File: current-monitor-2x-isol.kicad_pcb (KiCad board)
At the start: 2 copper layers, 35 x 44 mm, 34 parts, among them J1 CONN-2, J2 CONN-2, J3 USB-MICROB, J4 JTAG, U1 ACS711EX, U2 ACS711EX, U3 MKL26ZxxVFM4, Y1 12MHz

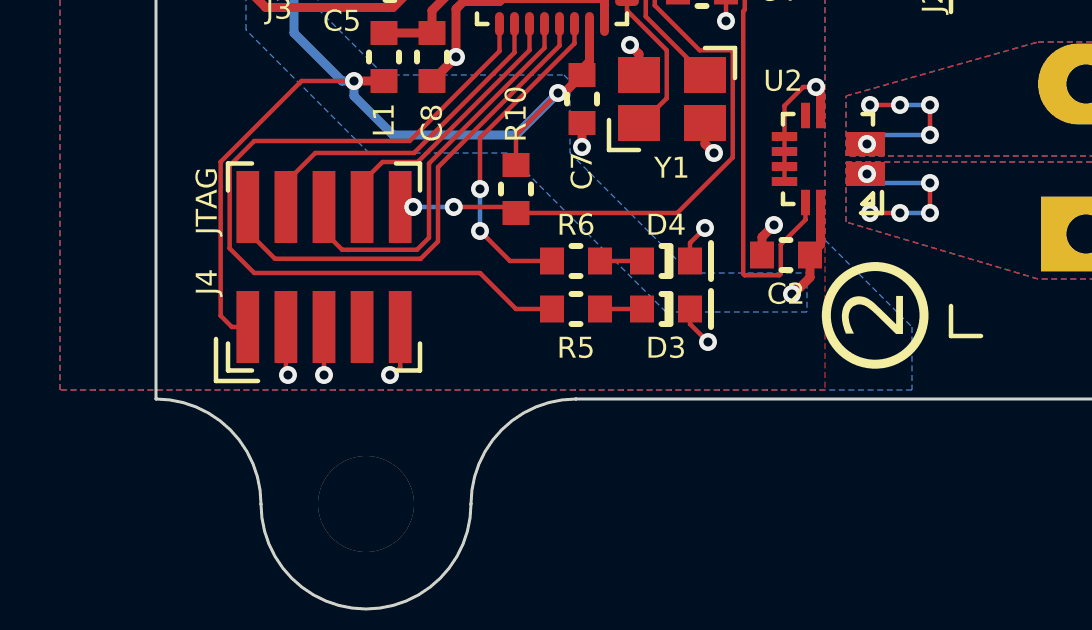
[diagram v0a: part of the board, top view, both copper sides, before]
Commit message: notes, small track change
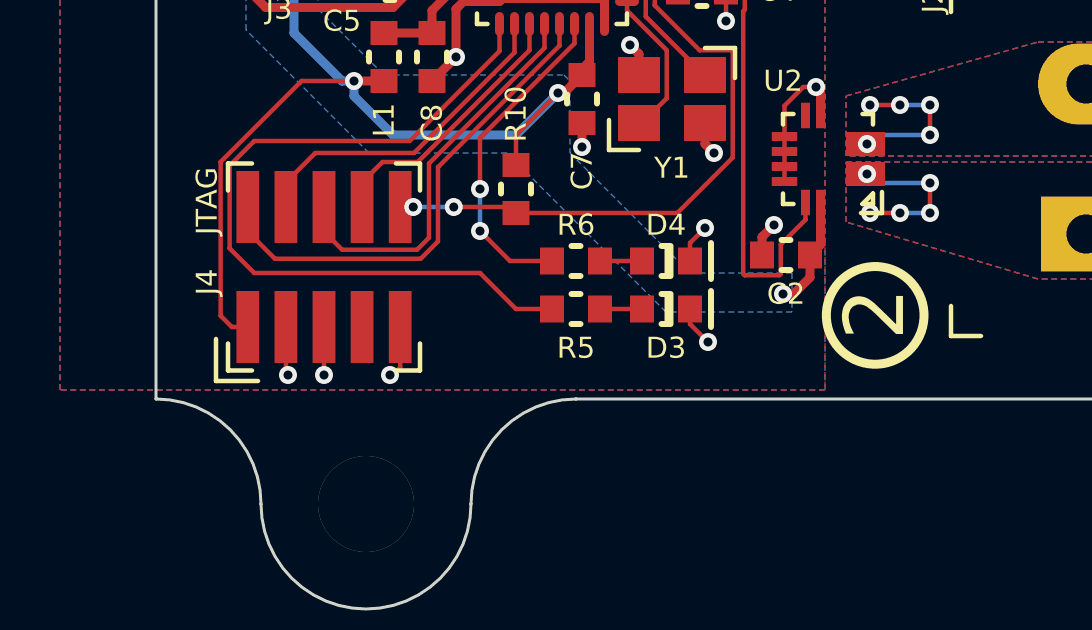
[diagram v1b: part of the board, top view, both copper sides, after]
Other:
- board text added: "70um/2oz copper"
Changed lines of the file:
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@@
     (links 97)
     (no_connects 0)
-    (area 162.949999 75.949999 198.050001 120.050001)
+    (area 109.35 75.799999 198.200001 120.200001)
     (thickness 1.6)
-    (drawings 14)
+    (drawings 15)
     (tracks 317)
     (zones 0)
@@
   (title_block
     (title "2x Isolated Current Monitor")
-    (date 2015-11-09)
+    (date 2015-11-12)
     (rev 1.0)
     (company sternlabs)
@@
     (pad 1 thru_hole circle (at 0 0 180) (size 3.2 3.2) (drill 3.2) (layers *.Cu *.Mask))
   )
+  (gr_text "70um/2oz copper" (at 109.5 83.5) (layer Cmts.User)
+    (effects (font (size 1.5 1.5) (thickness 0.3)) (justify left))
+  )
   (gr_arc (start 170 116.5) (end 173.5 116.5) (angle 180) (layer Edge.Cuts) (width 0.1))
   (gr_arc (start 177 116.5) (end 173.5 116.5) (angle 90) (layer Edge.Cuts) (width 0.1))
@@
   (gr_line (start 163 113) (end 163 83) (layer Edge.Cuts) (width 0.1))
   (gr_line (start 198 83) (end 198 113) (layer Edge.Cuts) (width 0.1))
+  (segment (start 184.25 109.5) (end 183.9 109.5) (width 0.3) (layer F.Cu) (net 1))
+  (segment (start 184.8 108.2) (end 184.8 108.95) (width 0.3) (layer F.Cu) (net 1))
+  (segment (start 184.8 108.95) (end 184.25 109.5) (width 0.3) (layer F.Cu) (net 1))
+  (via (at 183.9 109.5) (size 0.6) (drill 0.3) (layers F.Cu B.Cu) (net 1))
   (segment (start 184.35 95.4) (end 184.1 95.4) (width 0.3) (layer F.Cu) (net 1))
   (segment (start 184.8 94.95) (end 184.35 95.4) (width 0.3) (layer F.Cu) (net 1))
   (segment (start 184.8 94.2) (end 184.8 94.95) (width 0.3) (layer F.Cu) (net 1))
   (via (at 184.1 95.4) (size 0.6) (drill 0.3) (layers F.Cu B.Cu) (net 1))
-  (segment (start 184.25 109.5) (end 184.2 109.5) (width 0.3) (layer F.Cu) (net 1))
-  (segment (start 184.8 108.95) (end 184.25 109.5) (width 0.3) (layer F.Cu) (net 1))
-  (segment (start 184.8 108.2) (end 184.8 108.95) (width 0.3) (layer F.Cu) (net 1))
-  (via (at 184.2 109.5) (size 0.6) (drill 0.3) (layers F.Cu B.Cu) (net 1))
   (segment (start 185.15 106.45) (end 185.15 107.85) (width 0.3) (layer F.Cu) (net 1))
   (segment (start 185.15 107.85) (end 184.8 108.2) (width 0.3) (layer F.Cu) (net 1))
@@
     (polygon
       (pts
-        (xy 159.8 112.7) (xy 159.8 83.3) (xy 185.3 83.3) (xy 185.3 107.7) (xy 188.2 110.6)
-        (xy 188.2 112.7)
+        (xy 159.8 112.7) (xy 159.8 83.3) (xy 185.3 83.3) (xy 185.3 107.7) (xy 185.3 112.7)
       )
     )
@@
       (pts
         (xy 171.4 97) (xy 169 97) (xy 168.4 97.6) (xy 168.4 100) (xy 170.6 102.2)
-        (xy 176.6 102.2) (xy 176.8 102.4) (xy 176.8 104.8) (xy 180.8 108.8) (xy 184.7 108.8)
-        (xy 184.7 110.1) (xy 180 110.1) (xy 174.7 104.8) (xy 170.1 104.8) (xy 166 100.7)
+        (xy 176.6 102.2) (xy 176.8 102.4) (xy 176.8 104.8) (xy 180.8 108.8) (xy 184.2 108.8)
+        (xy 184.2 110.1) (xy 180 110.1) (xy 174.7 104.8) (xy 170.1 104.8) (xy 166 100.7)
         (xy 166 98) (xy 171.4 92.6) (xy 182.3 92.6) (xy 182.3 93.8) (xy 184.4 93.8)
         (xy 184.4 95.8) (xy 182.7 95.8) (xy 180.9 94) (xy 174.2 94) (xy 171.4 97)

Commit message: update to 1.1
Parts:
- removed Y1: 12MHz, libs:OSC3225
- added C9: 0.1u, libs:SMD-1608, F.Cu at (171.4, 98.4)
- added G***: LOGO, libs:starfish2-10, B.Cu at (176.5, 93.0)
- added SJ1: BOOT, libs:SMD-1005, F.Cu at (175.4, 103.6)
- added U4: MIC5365, libs:SC-70-5, F.Cu at (171.2, 89.3)
- C5, C6: value 2.2u -> 1.0u
- J1, J2: footprint libs:TERM-2-5.0-PTH -> libs:TERM-2-5.0-8.2-PTH
- R8, R9: value 22 -> 33
- U3: value MKL26ZxxVFM4 -> MKL27ZxxVFM4; footprint local:MKL26ZxxVFM4 -> libs:MKL27ZxxVFM4
- moved C6 11.0 mm to (171.2, 86.6), turned to 90 degrees
- moved C5 7.21 mm to (171.2, 92.0)
- moved R10 5.00 mm to (179.0, 103.0)
- moved J1 0.20 mm to (193.8, 91.0)
- moved J2 0.20 mm to (193.8, 105.0)
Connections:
- U3 pad 14: /LED2H -> /BOOT0CFG
- U3 pad 17: Net-(U3-Pad17) -> /LED2L
- U3 pad 18: Net-(U3-Pad18) -> /LED2H
- U3 pad 6: /VBUS -> (no net)
- U3 pad 9: /LED2L -> (no net)
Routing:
- net /LED2L: track 25.8 -> 13.5 mm
- net /VBUS: track 15.4 -> 9.70 mm
- net Net-(U3-Pad17): track 5.04 -> 0.00 mm
- net /LEDACT: track 13.6 -> 18.5 mm
- net Net-(U3-Pad18): track 4.36 -> 0.00 mm
- net COM: track 47.3 -> 50.6 mm, vias 21 -> 24
- net /BOOT0CFG: track 0.00 -> 3.24 mm
- net +3V3: track 47.9 -> 50.9 mm, vias 5 -> 8
- net /LED2H: track 11.0 -> 13.4 mm, vias 2 -> 0
- net /~RESET: track 20.5 -> 22.5 mm
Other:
- board text added: "Isolated Current Monitor"
- board text added: "sternlabs.org"
- board text added: "v1.1"

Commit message: small adjustments
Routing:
- net COM: track 50.6 -> 52.0 mm, vias 24 -> 25
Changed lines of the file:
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@@
     (thickness 1.6)
     (drawings 18)
-    (tracks 360)
+    (tracks 362)
     (zones 0)
     (modules 37)
@@
   (title_block
     (title "2x Isolated Current Monitor")
-    (date 2015-12-20)
+    (date 2015-12-21)
     (rev 1.1)
     (company sternlabs)
@@
   (module libs:SMD-1608 (layer F.Cu)
     (at 184 94.2 270)
-    (fp_text reference C1 (at -1.3 0 360) (layer F.SilkS)
+    (fp_text reference C1 (at 1.2 -0.4 360) (layer F.SilkS)
       (effects (font (size 0.7 0.7) (thickness 0.15)))
     )
@@
   (module libs:SMD-1608 (layer F.Cu)
     (at 180.4 93.8 180)
-    (fp_text reference C3 (at 0 2.5 270) (layer F.SilkS)
+    (fp_text reference C3 (at 0 2.1 270) (layer F.SilkS)
       (effects (font (size 0.7 0.7) (thickness 0.15)))
     )
@@
   (module libs:SMD-1608 (layer F.Cu)
     (at 181.2 99.4 90)
-    (fp_text reference C4 (at 0 2.5 180) (layer F.SilkS)
+    (fp_text reference C4 (at 0 2.2 180) (layer F.SilkS)
       (effects (font (size 0.7 0.7) (thickness 0.15)))
     )
@@
   (segment (start 177.45 100.5) (end 177.45 101.75) (width 0.3) (layer F.Cu) (net 1) (status 10))
   (segment (start 177.45 101.75) (end 177.2 102) (width 0.3) (layer F.Cu) (net 1) (status 20))
+  (segment (start 180.4 93) (end 180.4 92) (width 0.15) (layer F.Cu) (net 2))
+  (via (at 180.4 92) (size 0.6) (drill 0.3) (layers F.Cu B.Cu) (net 2))
+  (segment (start 179.4 94.375736) (end 179.4 94.8) (width 0.15) (layer F.Cu) (net 2))
+  (segment (start 180.35 93) (end 179.4 93.95) (width 0.15) (layer F.Cu) (net 2))
+  (segment (start 180.4 93) (end 180.35 93) (width 0.15) (layer F.Cu) (net 2))
+  (segment (start 179.4 93.95) (end 179.4 94.375736) (width 0.15) (layer F.Cu) (net 2))
+  (via (at 179.4 94.8) (size 0.6) (drill 0.3) (layers F.Cu B.Cu) (net 2))
   (segment (start 168.275736 90.4) (end 168.7 90.4) (width 0.15) (layer F.Cu) (net 2))
   (segment (start 168.05 90.4) (end 168.275736 90.4) (width 0.15) (layer F.Cu) (net 2))
@@
   (segment (start 183.2 93.6) (end 182.8 93.2) (width 0.3) (layer F.Cu) (net 2))
   (via (at 182.8 93.2) (size 0.6) (drill 0.3) (layers F.Cu B.Cu) (net 2))
-  (segment (start 179.4 93.975736) (end 179.4 94.4) (width 0.15) (layer F.Cu) (net 2))
-  (segment (start 179.4 93.95) (end 179.4 93.975736) (width 0.15) (layer F.Cu) (net 2))
-  (segment (start 180.35 93) (end 179.4 93.95) (width 0.15) (layer F.Cu) (net 2))
-  (segment (start 180.4 93) (end 180.35 93) (width 0.15) (layer F.Cu) (net 2))
-  (via (at 179.4 94.4) (size 0.6) (drill 0.3) (layers F.Cu B.Cu) (net 2))
   (via (at 168.3 95) (size 0.6) (drill 0.3) (layers F.Cu B.Cu) (net 2))
   (segment (start 167.125 96.1) (end 168.1 96.1) (width 0.3) (layer F.Cu) (net 2))
